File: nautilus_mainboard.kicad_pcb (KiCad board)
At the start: 4 copper layers, 176.2 x 77.5 mm, 105 parts, among them IC1 STM32H7B0RBT6, IC2 TCAN3414DRBR, IC3 TPS2121RUXT, IC4 TPS2121RUXT, IC5 TPS2121RUXT, J1 61300211121, J18 179-UJ20CHC4SMTTR, J2 61300211121, J3 1761681-3, J4 Header male 1x05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

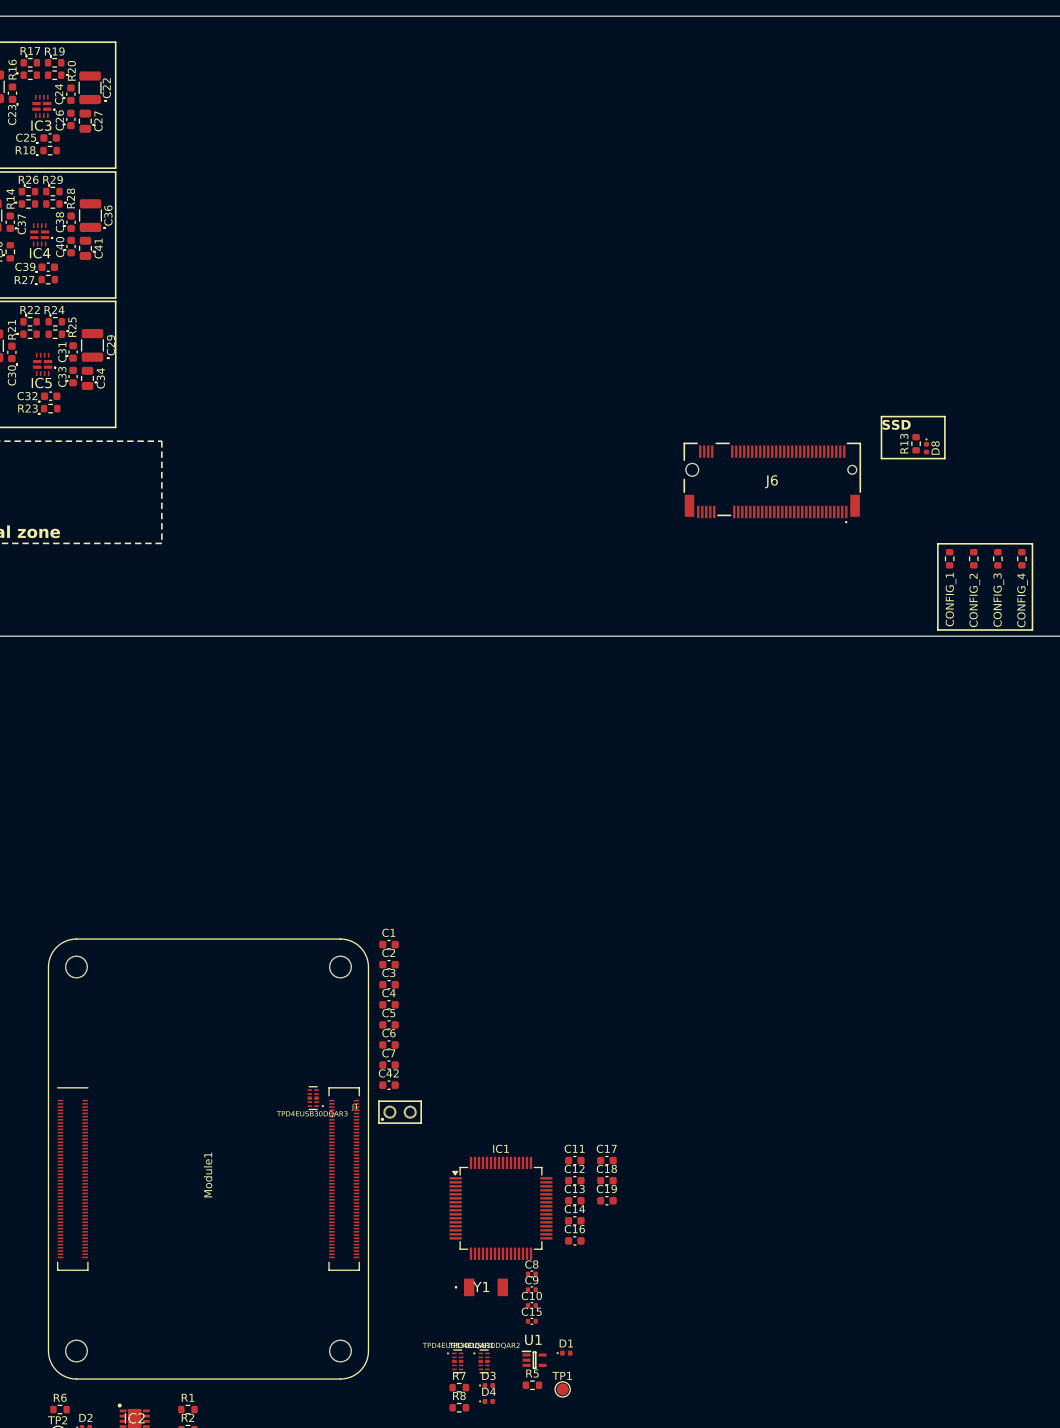
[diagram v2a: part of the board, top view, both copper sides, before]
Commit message: 4x accel and gyro, added pi stl
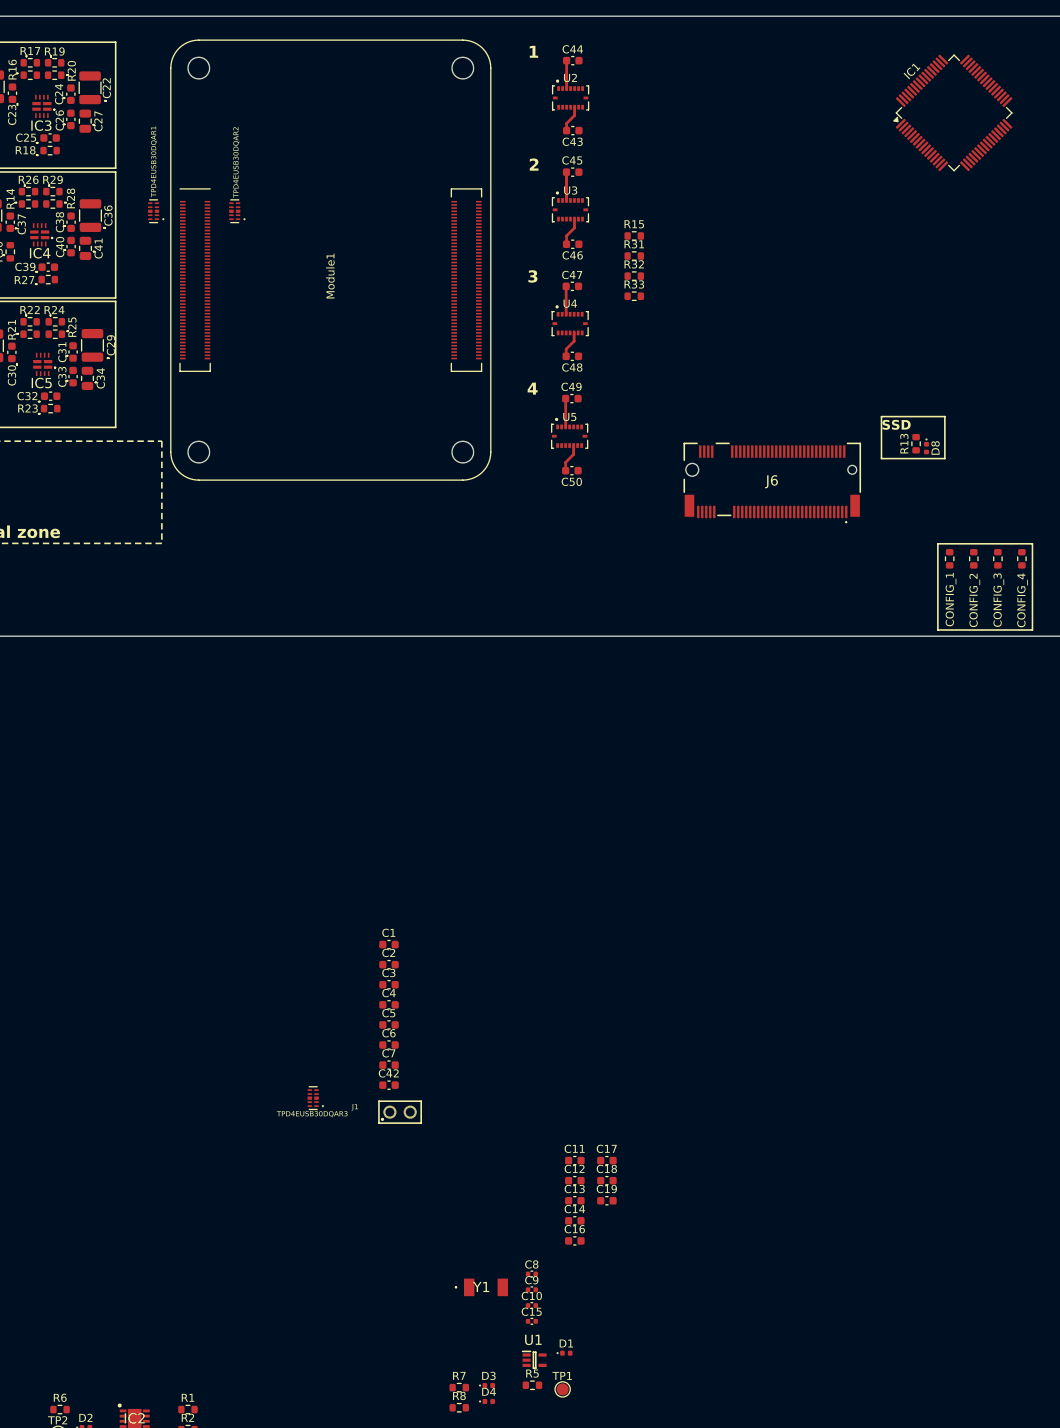
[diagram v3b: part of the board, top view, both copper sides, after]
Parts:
- added C43: 100nF, Capacitor_SMD:C_0603_1608Metric, F.Cu at (171.3, 61.8)
- added C44: 100nF, Capacitor_SMD:C_0603_1608Metric, F.Cu at (171.3, 53.1)
- added C45: 100nF, Capacitor_SMD:C_0603_1608Metric, F.Cu at (171.3, 67.0)
- added C46: 100nF, Capacitor_SMD:C_0603_1608Metric, F.Cu at (171.3, 76.0)
- added C47: 100nF, Capacitor_SMD:C_0603_1608Metric, F.Cu at (171.2, 81.3)
- added C48: 100nF, Capacitor_SMD:C_0603_1608Metric, F.Cu at (171.2, 90.0)
- added C49: 100nF, Capacitor_SMD:C_0603_1608Metric, F.Cu at (171.2, 95.3)
- added C50: 100nF, Capacitor_SMD:C_0603_1608Metric, F.Cu at (171.2, 104.3)
- added R15: 2.2k, Resistor_SMD:R_0603_1608Metric, F.Cu at (179.0, 75.0)
- added R31: 2.2k, Resistor_SMD:R_0603_1608Metric, F.Cu at (179.0, 77.5)
- added R32: 2.2k, Resistor_SMD:R_0603_1608Metric, F.Cu at (179.0, 80.0)
- added R33: 2.2k, Resistor_SMD:R_0603_1608Metric, F.Cu at (179.0, 82.5)
- added U2: 262-BMI088, dz_sens:Bosch_IMU_BMI088, F.Cu at (171.0, 57.7)
- added U3: 262-BMI088, dz_sens:Bosch_IMU_BMI088, F.Cu at (171.0, 71.7)
- added U4: 262-BMI088, dz_sens:Bosch_IMU_BMI088, F.Cu at (171.0, 85.9)
- added U5: 262-BMI088, dz_sens:Bosch_IMU_BMI088, F.Cu at (170.9, 100.0)
- moved TPD4EUSB30DQAR1 148.7 mm to (118.9, 71.9), turned to 180 degrees
- moved IC1 148.2 mm to (219.0, 59.6), turned to 45 degrees
- moved TPD4EUSB30DQAR2 147.1 mm to (129.0, 71.9), turned to 180 degrees
- moved Module1 113.4 mm to (124.5, 102.0)
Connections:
- net STM_IN_3.3V renamed BMI_IN_3.3V
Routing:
- net BMI_IN_3.3V: track 0.00 -> 31.4 mm
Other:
- board text added: "1"
- board text added: "2"
- board text added: "3"
- board text added: "4"

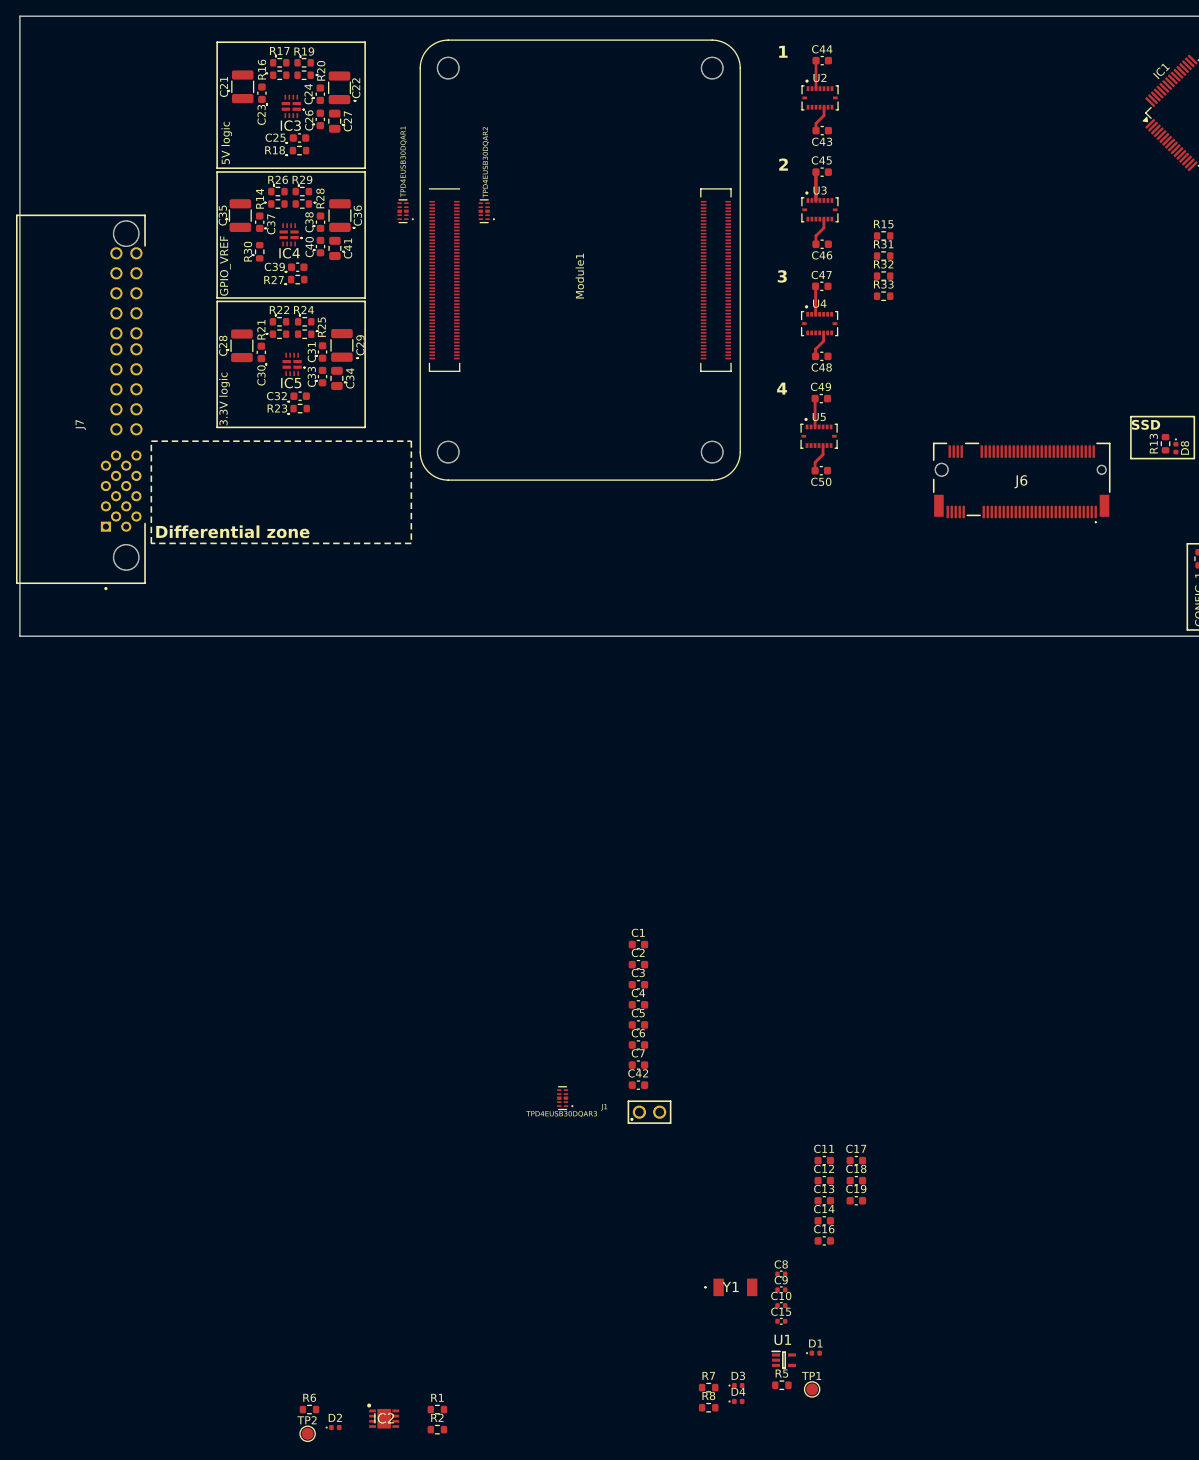
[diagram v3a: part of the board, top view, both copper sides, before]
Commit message: new outline of board plus first traces
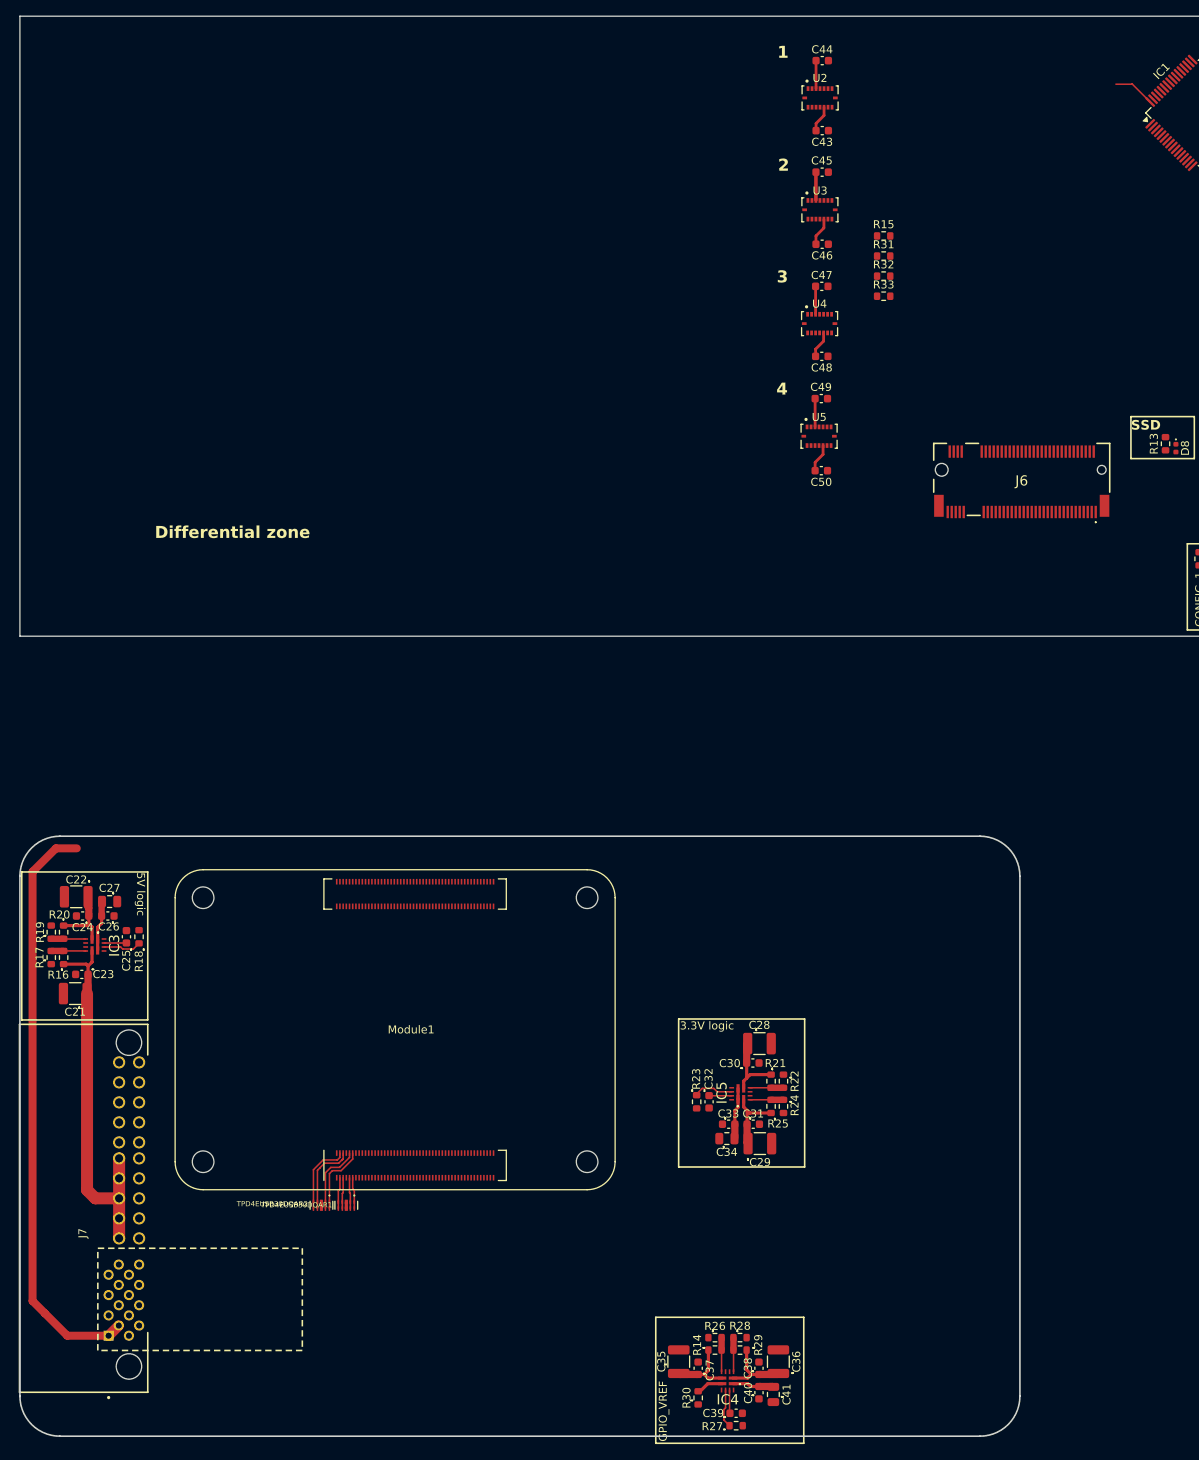
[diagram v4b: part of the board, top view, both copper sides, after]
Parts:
- removed C1, C11, C19, C2, C3, C4, C5, C6: 100nF, Capacitor_SMD:C_0603_1608Metric
- removed C10, C15: 2.2pF, Capacitor_SMD:C_0402_1005Metric
- removed C12, C13, C14, C16, C17, C18: 10pF, Capacitor_SMD:C_0603_1608Metric
- removed C42, C7: 1uF, Capacitor_SMD:C_0603_1608Metric
- removed C8, C9: 4.7pF, Capacitor_SMD:C_0402_1005Metric
- removed D1: APHHS1005LSECK/J3-PF, LED_SMD:LED_0402_1005Metric
- removed D2, D4: APHHS1005LZGCK-V, LED_SMD:LED_0402_1005Metric
- removed D3: APHHS1005LSYCK/J3-PF, LED_SMD:LED_0402_1005Metric
- removed IC2: TCAN3414DRBR, dz_comm:TCAN3414DRBR
- removed J1: 61300211121, dz_con:Wurth_Con_61300211121
- removed R1: 2.2k, Resistor_SMD:R_0603_1608Metric
- removed R2: 4.3k, Resistor_SMD:R_0603_1608Metric
- removed R5, R6, R7, R8: 1k, Resistor_SMD:R_0603_1608Metric
- removed TP1, TP2: Test Point, TestPoint:TestPoint_Pad_D1.5mm
- removed TPD4EUSB30DQAR3: ~, dz_con:IC_TPD4EUSB30DQAR
- removed U1: Buffers & Line Driver, dz_dio:SOT65P210X110-5N
- removed Y1: CC4V-T1A-32.768kHz-6pF-20PPM-TA-QC, dz_sens:CC4VT1A
- moved R29 154.8 mm to (161.0, 214.2)
- moved C35 153.4 mm to (153.4, 215.7)
- moved C36 153.4 mm to (165.8, 215.7)
- moved C37 153.4 mm to (155.8, 216.5)
- moved C38 153.4 mm to (163.4, 216.5)
- moved C39 153.4 mm to (160.5, 222.1)
- moved C40 153.4 mm to (163.4, 219.6)
- moved C41 153.4 mm to (165.2, 219.8)
- moved IC4 153.4 mm to (159.5, 218.1)
- moved R27 153.4 mm to (160.5, 223.7)
- moved R30 153.4 mm to (155.8, 220.2)
- moved R14 153.3 mm to (157.9, 214.2)
- moved R26 153.3 mm to (157.9, 212.7)
- moved R28 151.9 mm to (161.0, 212.7)
- moved TPD4EUSB30DQAR2 125.9 mm to (108.7, 196.1), turned to -90 degrees
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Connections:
- C28 pad 2: Net-(IC5-OV1) -> GND
- C30 pad 2: Net-(IC5-OV1) -> GND
- IC5 pad 5: Net-(IC5-OV1) -> GND
- R22 pad 1: Net-(IC5-OV1) -> GND
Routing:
- net Battery_Out_3.3V: track 0.00 -> 82.5 mm
- net Battery_Out_5V: track 0.00 -> 47.8 mm
- net BMI_IN_3.3V: track 31.4 -> 52.0 mm
- net /CM4/CM4_Module1A/TRD1_N: track 0.00 -> 9.52 mm
- net /CM4/CM4_Module1A/TRD1_P: track 0.00 -> 9.35 mm
- net CM4_LED_IN_3.3V: track 0.00 -> 9.20 mm
- net STM_Plug_3.3V: track 0.00 -> 8.91 mm
- net /CM4/CM4_Module1A/TRD0_N: track 0.00 -> 8.83 mm
- net USB_Out_5V: track 0.00 -> 8.80 mm
- net /CM4/CM4_Module1A/TRD0_P: track 0.00 -> 8.78 mm
- net GPIO_VREF_3.3V: track 0.00 -> 8.61 mm
- net CM4_IN_5V: track 0.00 -> 6.33 mm
- net Net-(IC5-ILIM): track 0.00 -> 4.99 mm
- net Net-(IC4-ILIM): track 0.00 -> 4.82 mm
- net Net-(IC3-ILIM): track 0.00 -> 4.77 mm
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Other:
- board size 176.2 x 77.5 mm -> 176.2 x 177.5 mm

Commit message: ignore
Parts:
- removed J6: MDT275M02001, dz_con:PCIE_MDT275M02001
- moved Module1 8.20 mm to (149.9, 192.3)
- moved TPD4EUSB30DQAR1 8.20 mm to (119.8, 197.8)
- moved TPD4EUSB30DQAR2 8.20 mm to (116.7, 197.8)
